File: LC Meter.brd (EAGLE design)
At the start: 99.9 x 71 mm, 38 parts, among them IC1 PIC16F628SO

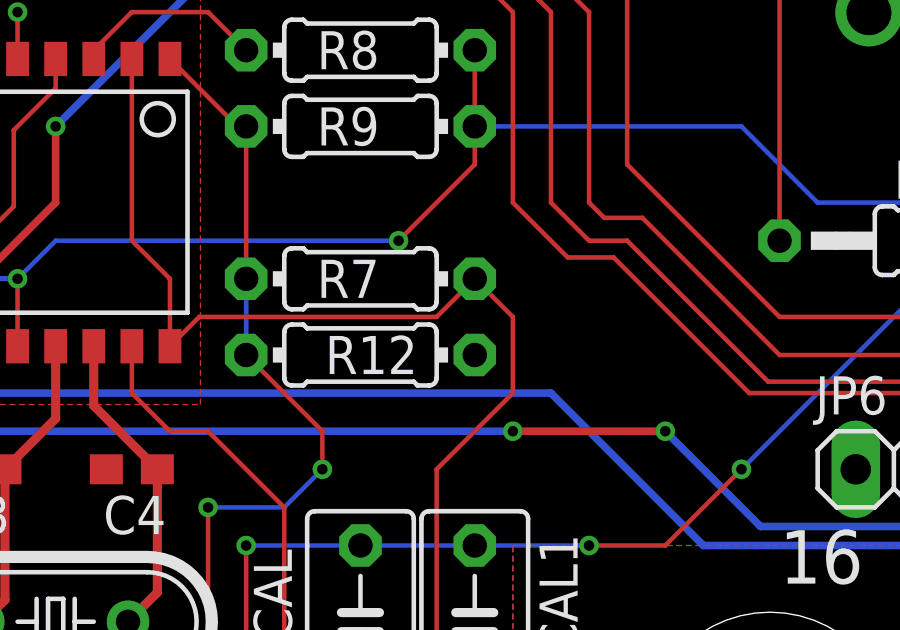
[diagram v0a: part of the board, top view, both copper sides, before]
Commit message: Fix for iCloud symlink issue
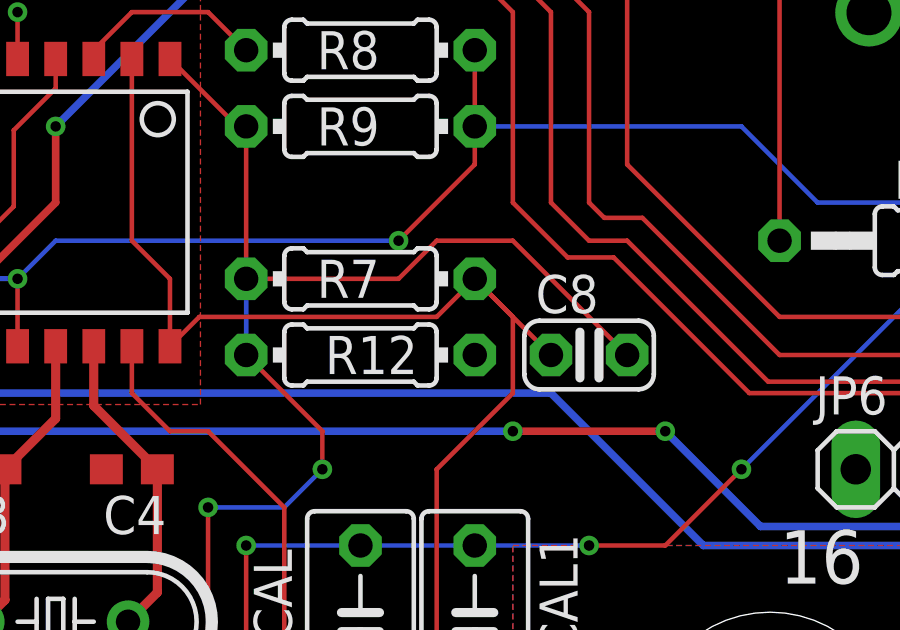
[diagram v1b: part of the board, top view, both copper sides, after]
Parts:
- added C8: 10pF, rcl:C025-024X044
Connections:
- net RA2: now also C8.2
- net RA3: now also C8.1
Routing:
- net RA2: track 30.1 -> 44.9 mm
- net RA3: track 41.8 -> 45.4 mm
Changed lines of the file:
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@@
 <grid distance="50" unitdist="mil" unit="mil" style="lines" multiple="1" display="no" altdistance="5" altunitdist="mil" altunit="mil"/>
 <layers>
-<layer number="1" name="Top" color="4" fill="1" visible="no" active="yes"/>
+<layer number="1" name="Top" color="4" fill="1" visible="yes" active="yes"/>
 <layer number="2" name="Route2" color="16" fill="1" visible="no" active="no"/>
 <layer number="3" name="Route3" color="17" fill="1" visible="no" active="no"/>
@@
 <layer number="19" name="Unrouted" color="6" fill="1" visible="yes" active="yes"/>
 <layer number="20" name="Dimension" color="24" fill="1" visible="yes" active="yes"/>
-<layer number="21" name="tPlace" color="7" fill="1" visible="no" active="yes"/>
+<layer number="21" name="tPlace" color="7" fill="1" visible="yes" active="yes"/>
 <layer number="22" name="bPlace" color="7" fill="1" visible="yes" active="yes"/>
-<layer number="23" name="tOrigins" color="15" fill="1" visible="no" active="yes"/>
+<layer number="23" name="tOrigins" color="15" fill="1" visible="yes" active="yes"/>
 <layer number="24" name="bOrigins" color="15" fill="1" visible="yes" active="yes"/>
 <layer number="25" name="tNames" color="7" fill="1" visible="yes" active="yes"/>
@@
 <attribute name="VALUE" x="15.875" y="52.07" size="1.27" layer="28" rot="MR270"/>
 </element>
+<element name="C8" library="rcl" library_urn="urn:adsk.eagle:library:334" package="C025-024X044" package3d_urn="urn:adsk.eagle:package:23630/1" value="10pF" x="41.91" y="46.99" smashed="yes">
+<attribute name="NAME" x="40.132" y="48.387" size="1.27" layer="25" ratio="10"/>
+<attribute name="POPULARITY" value="17" x="41.91" y="46.99" size="1.778" layer="27" display="off"/>
+<attribute name="SPICEPREFIX" value="C" x="41.91" y="46.99" size="1.778" layer="27" display="off"/>
+<attribute name="VALUE" x="40.132" y="44.323" size="1.27" layer="27" ratio="10"/>
+</element>
 </elements>
 <signals>
@@
 <wire x1="38.735" y1="32.385" x2="39.878" y2="32.385" width="0.1524" layer="1"/>
 <wire x1="39.37" y1="45.72" x2="36.83" y2="43.18" width="0.1524" layer="1"/>
+<contactref element="C8" pad="1"/>
+<wire x1="40.64" y1="46.99" x2="38.1" y2="49.53" width="0.1524" layer="1"/>
 </signal>
 <signal name="RA4">
@@
 <wire x1="29.21" y1="41.91" x2="29.21" y2="35.306" width="0.1524" layer="1"/>
 <wire x1="29.21" y1="35.306" x2="26.924" y2="33.02" width="0.1524" layer="1"/>
+<contactref element="C8" pad="2"/>
+<wire x1="43.18" y1="46.99" x2="39.37" y2="50.8" width="0.1524" layer="1"/>
+<wire x1="39.37" y1="50.8" x2="36.83" y2="50.8" width="0.1524" layer="1"/>
+<wire x1="36.83" y1="50.8" x2="35.56" y2="49.53" width="0.1524" layer="1"/>
+<wire x1="35.56" y1="49.53" x2="30.48" y2="49.53" width="0.1524" layer="1"/>
 </signal>
 <signal name="N$1">
